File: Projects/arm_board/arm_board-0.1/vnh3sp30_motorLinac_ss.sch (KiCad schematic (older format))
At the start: 6 parts, among them P9 CONN_4X2, U57 74HC08

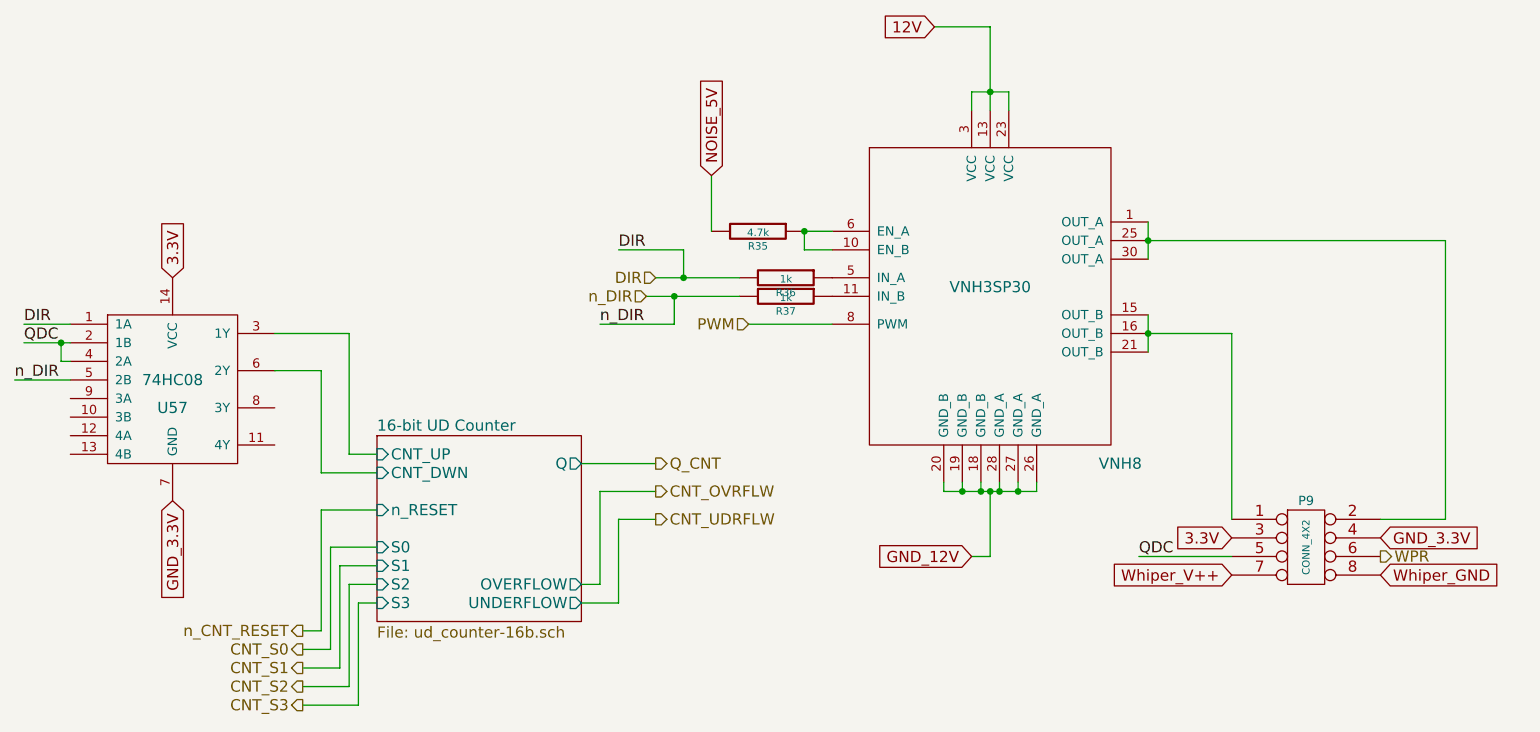
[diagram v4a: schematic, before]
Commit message: Arm Board: finalizing footprints.
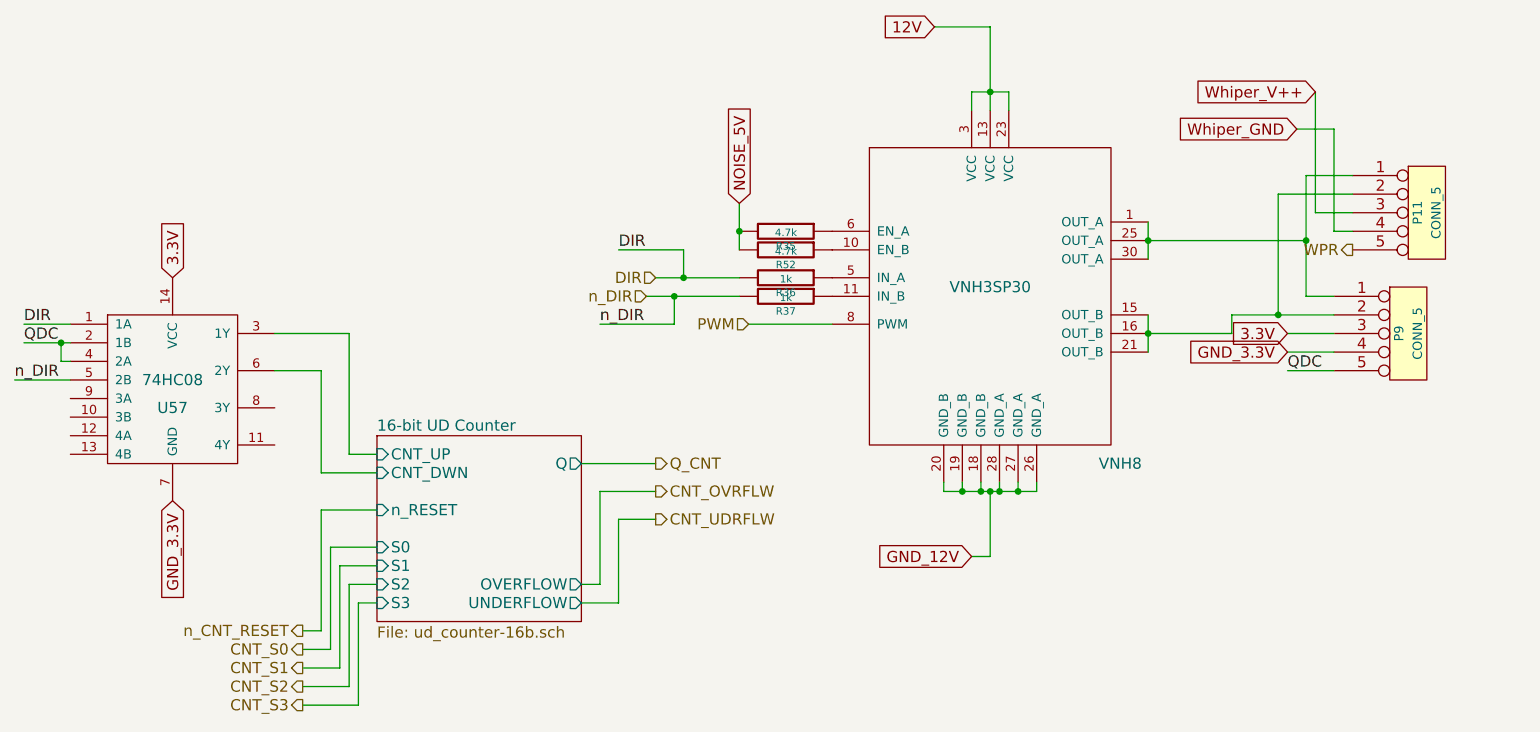
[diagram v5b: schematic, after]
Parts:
- removed P9: CONN_4X2, ArmFootprints:MiniFitJr_8-pin_0050348563, symbol CONN_4X2
- added P11, P9: CONN_5, ArmFootprints:5-pin_640467-1, symbol CONN_5
- added R52: 4.7k, Resistors_SMD:R_0805, symbol R
- U57: footprint SMD_Packages:SOIC-14_N -> ArmFootprints:SOIC-14
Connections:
- net 3.3V: now also P9.3
- net GND_3.3V: now also P9.4
- net NOISE_5V: now also R52.2
- net QDC: now also P9.5
- net WPR: now also P11.5
- net Whiper_GND: now also P11.4
- net Whiper_V++: now also P11.3
- net at VNH8.1 (OUT_A), VNH8.25 (OUT_A), VNH8.30 (OUT_A): now also P11.1, P9.1
- net at R35.1, VNH8.6 (EN_A): no longer VNH8.10 (EN_B)
- net at VNH8.15 (OUT_B), VNH8.16 (OUT_B), VNH8.21 (OUT_B): now also P11.2, P9.2
- new net: R52.1, VNH8.10 (EN_B)
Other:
- moved on the sheet: R35
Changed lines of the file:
@@
 	9400 3950 9400 4150
 Connection ~ 9400 4050
-Text Label 9350 5250 0    60   ~ 0
+Text Label 10150 4250 0    60   ~ 0
 QDC
-Text GLabel 9850 5350 0    60   Input ~ 0
+Text GLabel 10300 2750 0    60   Input ~ 0
 Whiper_V++
-Wire Wire Line
-	9400 3550 11000 3550
-Text HLabel 10650 5250 2    60   Output ~ 0
+Text HLabel 10500 3600 0    60   Output ~ 0
 WPR
-Text GLabel 10650 5350 2    60   Input ~ 0
+Text GLabel 10200 2950 0    60   Input ~ 0
 Whiper_GND
 $Comp
@@
 	6850 4000 6850 3850
 Connection ~ 6850 3850
-Text GLabel 7050 3200 1    60   Input ~ 0
+Text GLabel 7200 3350 1    60   Input ~ 0
 NOISE_5V
-Connection ~ 7550 3500
-Wire Wire Line
-	7550 3600 7550 3500
-Wire Wire Line
-	7700 3600 7550 3600
-Wire Wire Line
-	7550 3500 7700 3500
 $Comp
 L R R35
 U 1 1 56C65444
-P 7300 3500
-F 0 "R35" V 7380 3500 40  0000 C CNN
-F 1 "4.7k" V 7307 3501 40  0000 C CNN
-F 2 "Resistors_SMD:R_0805" V 7230 3500 30  0001 C CNN
-F 3 "" H 7300 3500 30  0000 C CNN
-	1    7300 3500
+P 7450 3500
+F 0 "R35" V 7530 3500 40  0000 C CNN
+F 1 "4.7k" V 7457 3501 40  0000 C CNN
+F 2 "Resistors_SMD:R_0805" V 7380 3500 30  0001 C CNN
+F 3 "" H 7450 3500 30  0000 C CNN
+	1    7450 3500
 	0    1    1    0
 $EndComp
-Wire Wire Line
-	7050 3200 7050 3500
-Text GLabel 9850 5150 0    60   Input ~ 0
+Text GLabel 10150 4050 0    60   Input ~ 0
 3.3V
-Text GLabel 10650 5150 2    60   Input ~ 0
+Text GLabel 10150 4150 0    60   Input ~ 0
 GND_3.3V
-$Comp
-L CONN_4X2 P9
-U 1 1 56C67526
-P 10250 5200
-F 0 "P9" H 10250 5450 50  0000 C CNN
-F 1 "CONN_4X2" V 10250 5200 40  0000 C CNN
-F 2 "ArmFootprints:MiniFitJr_8-pin_0050348563" H 10250 5200 60  0001 C CNN
-F 3 "" H 10250 5200 60  0000 C CNN
-	1    10250 5200
-	1    0    0    -1
-$EndComp
-Wire Wire Line
-	9850 4050 9850 5050
-Wire Wire Line
-	9350 5250 9850 5250
 Wire Wire Line
 	9400 4050 9850 4050
-Wire Wire Line
-	11000 3550 11000 5050
-Wire Wire Line
-	11000 5050 10650 5050
 $Comp
 L 74HC08 U57
@@
 F 0 "U57" H 4150 4150 60  0000 C CNN
 F 1 "74HC08" H 4150 4300 60  0000 C CNN
-F 2 "SMD_Packages:SOIC-14_N" H 4150 4300 60  0001 C CNN
+F 2 "ArmFootprints:SOIC-14" H 4150 4300 60  0001 C CNN
 F 3 "" H 4150 4300 60  0000 C CNN
 	1    4150 4300
@@
 Wire Wire Line
 	4950 4800 5250 4800
+$Comp
+L R R52
+U 1 1 56E605F6
+P 7450 3600
+F 0 "R52" V 7530 3600 40  0000 C CNN
+F 1 "4.7k" V 7457 3601 40  0000 C CNN
+F 2 "Resistors_SMD:R_0805" V 7380 3600 30  0001 C CNN
+F 3 "" H 7450 3600 30  0000 C CNN
+	1    7450 3600
+	0    1    1    0
+$EndComp
+Wire Wire Line
+	7200 3350 7200 3600
+Connection ~ 7200 3500
+$Comp
+L CONN_5 P9
+U 1 1 56E63D67
+P 10800 4050
+F 0 "P9" V 10750 4050 50  0000 C CNN
+F 1 "CONN_5" V 10850 4050 50  0000 C CNN
+F 2 "ArmFootprints:5-pin_640467-1" H 10800 4050 60  0001 C CNN
+F 3 "" H 10800 4050 60  0000 C CNN
+	1    10800 4050
+	1    0    0    -1
+$EndComp
+$Comp
+L CONN_5 P11
+U 1 1 56E63DFC
+P 10900 3400
+F 0 "P11" V 10850 3400 50  0000 C CNN
+F 1 "CONN_5" V 10950 3400 50  0000 C CNN
+F 2 "ArmFootprints:5-pin_640467-1" H 10900 3400 60  0001 C CNN
+F 3 "" H 10900 3400 60  0000 C CNN
+	1    10900 3400
+	1    0    0    -1
+$EndComp
+Wire Wire Line
+	10250 3200 10250 3850
+Wire Wire Line
+	10250 3850 10400 3850
+Connection ~ 10250 3550
+Wire Wire Line
+	9400 3550 10250 3550
+Wire Wire Line
+	9850 4050 9850 3950
+Wire Wire Line
+	9850 3950 10400 3950
+Wire Wire Line
+	10150 4050 10400 4050
+Wire Wire Line
+	10150 4150 10400 4150
+Wire Wire Line
+	10150 4250 10400 4250
+Wire Wire Line
+	10250 3200 10500 3200
+Wire Wire Line
+	10100 3950 10100 3300
+Wire Wire Line
+	10100 3300 10500 3300
+Connection ~ 10100 3950
+Wire Wire Line
+	10300 2750 10300 3400
+Wire Wire Line
+	10300 3400 10500 3400
+Wire Wire Line
+	10200 2950 10400 2950
+Wire Wire Line
+	10400 2950 10400 3500
+Wire Wire Line
+	10400 3500 10500 3500
 $EndSCHEMATC
